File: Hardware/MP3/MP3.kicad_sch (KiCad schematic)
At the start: 1 part, among them J1 Conn_02x20_Odd_Even

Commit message: Schematic notes
- notes regarding schematic layout and included ICs
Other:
- note added: "RPI -> DAC -> amplifier -> headphone jack -> 3/4 SDcards -> Rotary encoder"
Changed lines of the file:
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@@
 	(generator_version "9.0")
 	(paper "A4")
+	(text "RPI -> DAC -> amplifier -> headphone jack\n	-> 3/4 SDcards\n	-> Rotary encoder\n"
+		(exclude_from_sim no)
+		(at 166.116 47.498 0)
+		(effects
+			(font
+				(size 1.27 1.27)
+			)
+		)
+	)
 	(text "SPI pinouts can be unreliable, double triple check to make sure that they are correct"
 		(exclude_from_sim no)

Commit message: Large symbol import
- 5V boost
- Battery charger IC
- USB behaviour IC
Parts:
- added Pogo_pin_USB(OTG)1: Conn_01x02_Male, Connector_PinHeader_2.54mm:PinHeader_1x02_P2.54mm_Vertical, symbol Connector:Conn_01x02_Male
- J1: footprint (none) -> Connector_PinHeader_2.54mm:PinHeader_2x20_P2.54mm_Vertical
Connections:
- new net Data+: Pogo_pin_USB(OTG)1.1 (Pin_1)
- new net Data-: Pogo_pin_USB(OTG)1.2 (Pin_2)
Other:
- added sheet Power (power.kicad_sch)
- added sheet USB-C (USB.kicad_sch)

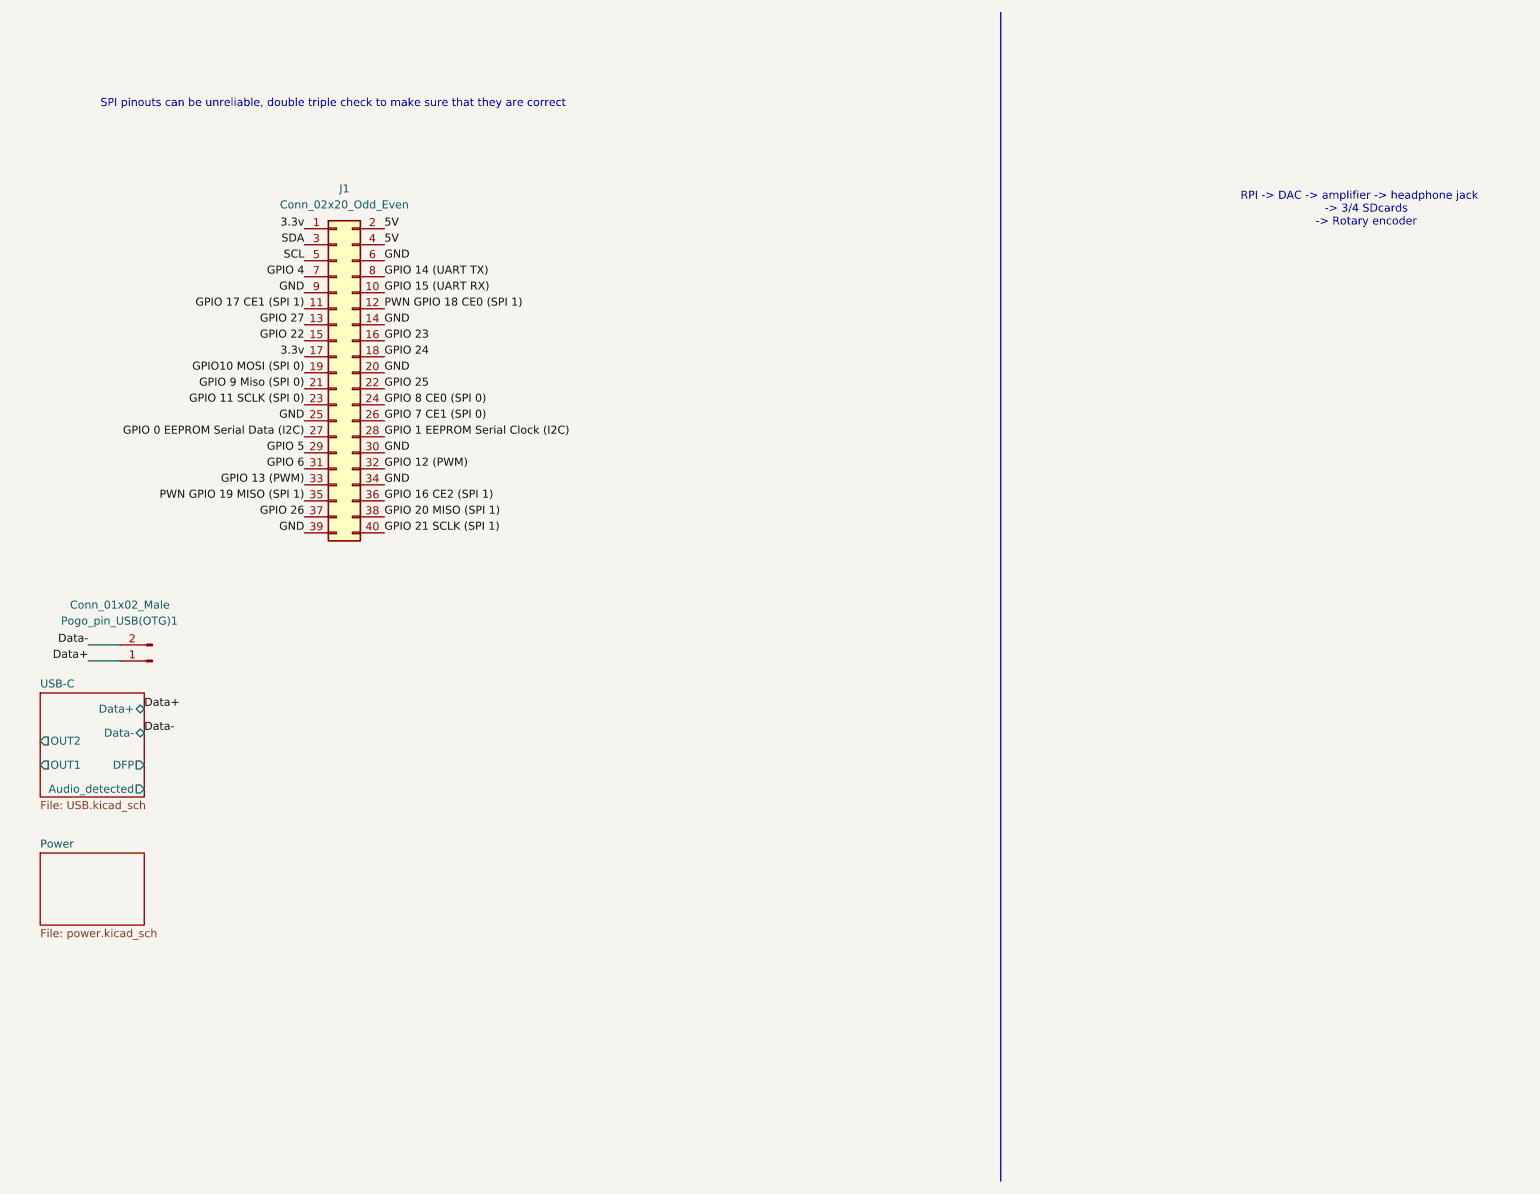
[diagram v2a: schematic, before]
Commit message: Large additions, DAC schematic work started
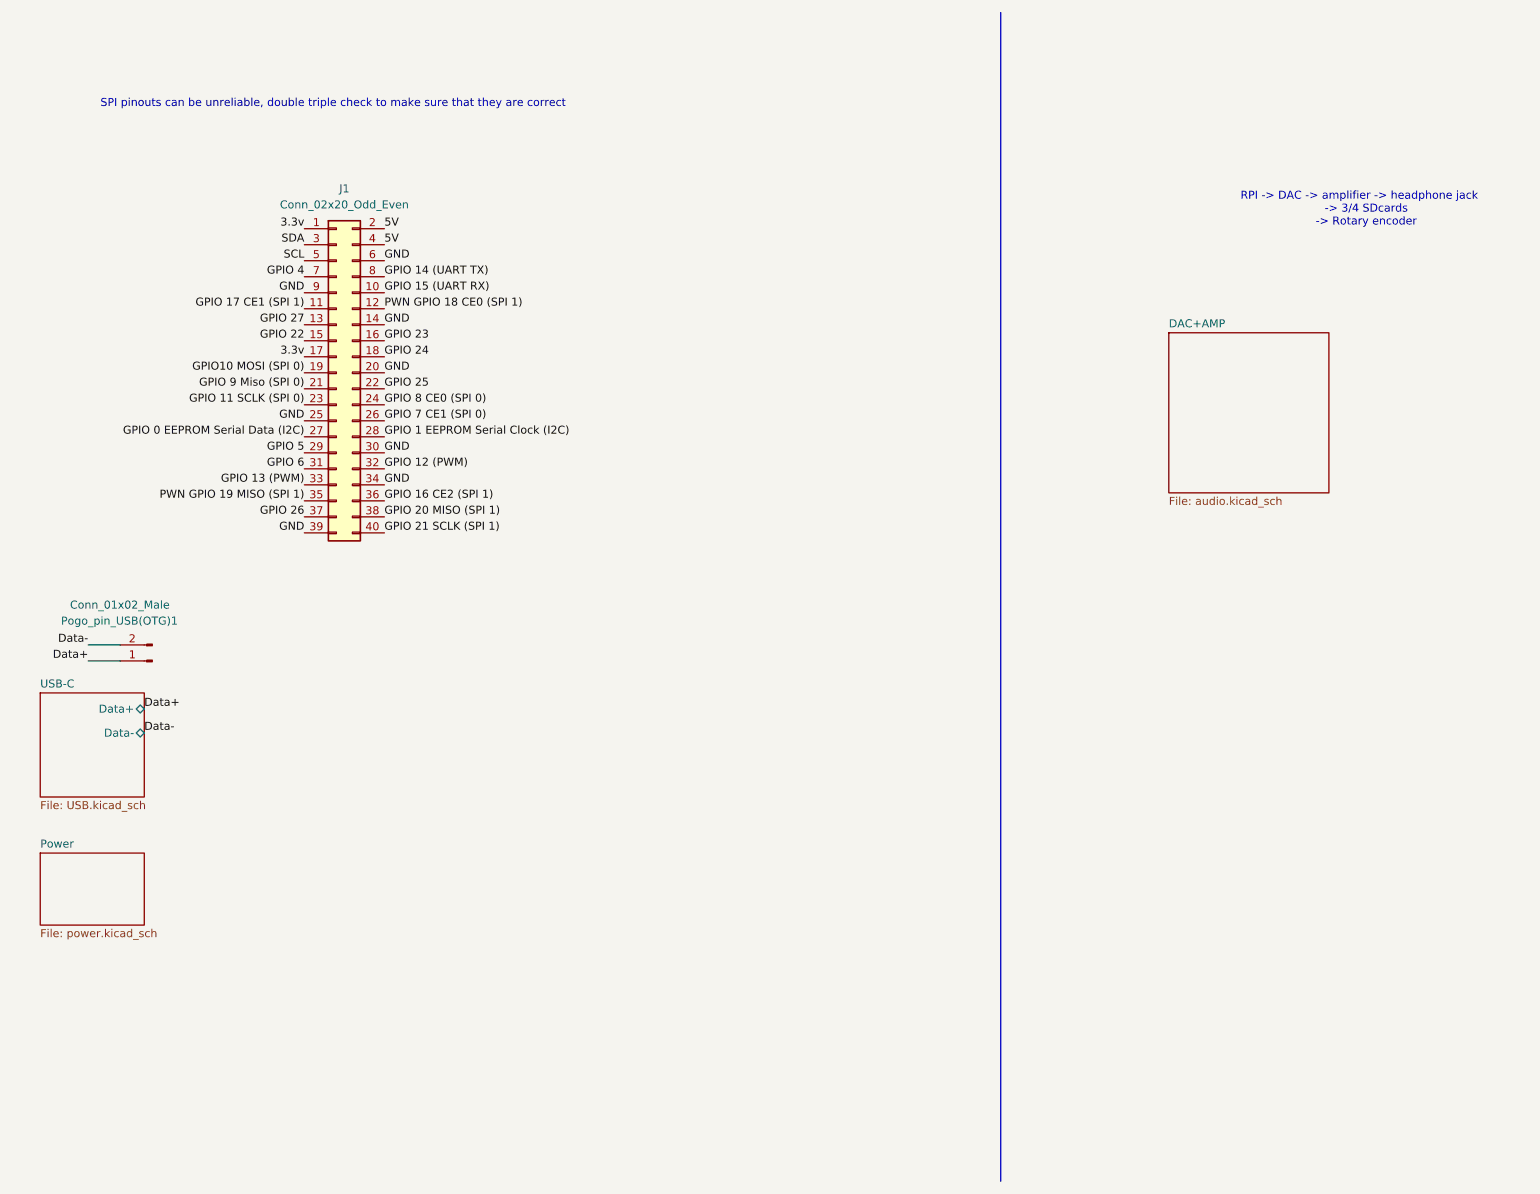
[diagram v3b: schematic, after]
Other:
- added sheet DAC+AMP (audio.kicad_sch)
- sheet USB-C ports: added none; removed Audio_detected, DFP, OUT1, OUT2
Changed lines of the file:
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@@
+	)
+	(sheet
+		(at 203.2 63.5)
+		(size 25.4 25.4)
+		(exclude_from_sim no)
+		(in_bom yes)
+		(on_board yes)
+		(dnp no)
+		(fields_autoplaced yes)
+		(stroke
+			(width 0.1524)
+			(type solid)
+		)
+		(fill
+			(color 0 0 0 0.0000)
+		)
+		(property "Sheetname" "DAC+AMP"
+			(at 203.2 62.7884 0)
+			(effects
+				(font
+					(size 1.27 1.27)
+				)
+				(justify left bottom)
+			)
+		)
+		(property "Sheetfile" "audio.kicad_sch"
+			(at 203.2 89.4846 0)
+			(effects
+				(font
+					(size 1.27 1.27)
+				)
+				(justify left top)
+			)
+		)
+		(instances
+			(project "MP3"
+				(path "/0e2978a4-9114-4e8f-a3b0-a18c9ec8fe33"
+					(page "4")
+				)
+			)
+		)
 	)
 	(sheet
@@
 			)
 		)
-		(pin "Audio_detected" output
-			(at 40.64 135.89 0)
-			(effects
-				(font
-					(size 1.27 1.27)
-				)
-				(justify right)
-			)
-		)
-		(pin "DFP" output
-			(at 40.64 132.08 0)
-			(effects
-				(font
-					(size 1.27 1.27)
-				)
-				(justify right)
-			)
-		)
-		(pin "OUT1" output
-			(at 24.13 132.08 180)
-			(effects
-				(font
-					(size 1.27 1.27)
-				)
-				(justify left)
-			)
-		)
-		(pin "OUT2" output
-			(at 24.13 128.27 180)
-			(effects
-				(font
-					(size 1.27 1.27)
-				)
-				(justify left)
-			)
-		)

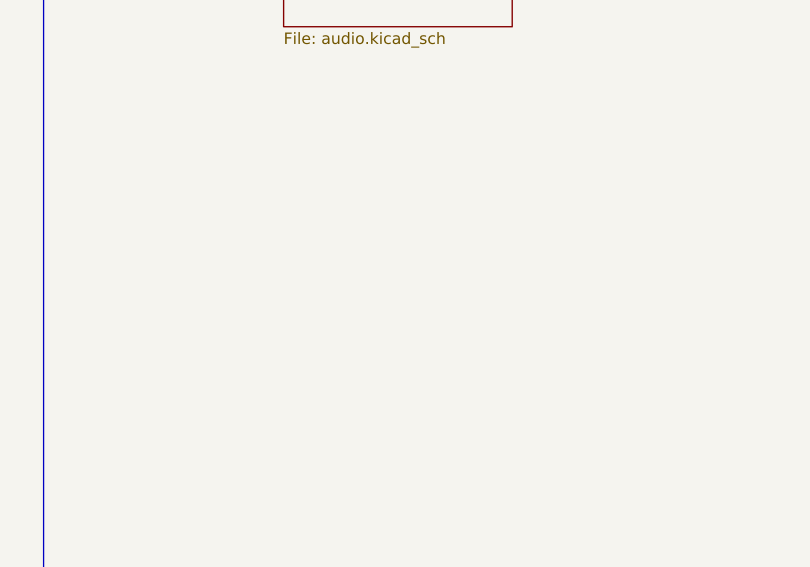
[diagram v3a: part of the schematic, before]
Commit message: feat: Made some changes to the DAC. Explicitly using register control (using I2C) with PCM audio. Planning to use 5.2V buck on 5V line, then Low noise LDO VREF for DAC, another for AMP power, and a 3v3 low noise LDO for DAC too.
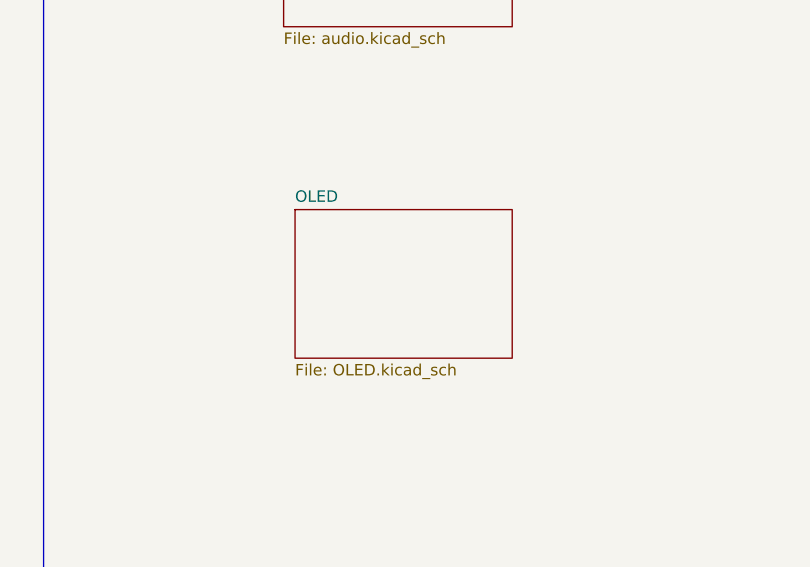
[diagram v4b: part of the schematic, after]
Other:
- added sheet OLED (OLED.kicad_sch)
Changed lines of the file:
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@@
+		)
+	)
+	(sheet
+		(at 204.47 109.22)
+		(size 24.13 16.51)
+		(exclude_from_sim no)
+		(in_bom yes)
+		(on_board yes)
+		(dnp no)
+		(fields_autoplaced yes)
+		(stroke
+			(width 0.1524)
+			(type solid)
+		)
+		(fill
+			(color 0 0 0 0.0000)
+		)
+		(property "Sheetname" "OLED"
+			(at 204.47 108.5084 0)
+			(effects
+				(font
+					(size 1.27 1.27)
+				)
+				(justify left bottom)
+			)
+		)
+		(property "Sheetfile" "OLED.kicad_sch"
+			(at 204.47 126.3146 0)
+			(effects
+				(font
+					(size 1.27 1.27)
+				)
+				(justify left top)
+			)
+		)
+		(instances
+			(project "MP3"
+				(path "/0e2978a4-9114-4e8f-a3b0-a18c9ec8fe33"
+					(page "5")
+				)
+			)
 		)
 	)
